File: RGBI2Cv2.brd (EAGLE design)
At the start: 37.8 x 50.8 mm, 10 parts, among them Q1 STP16NF06, Q2 STP16NF06, Q3 STP16NF06, U2 ATTINY45-20PU

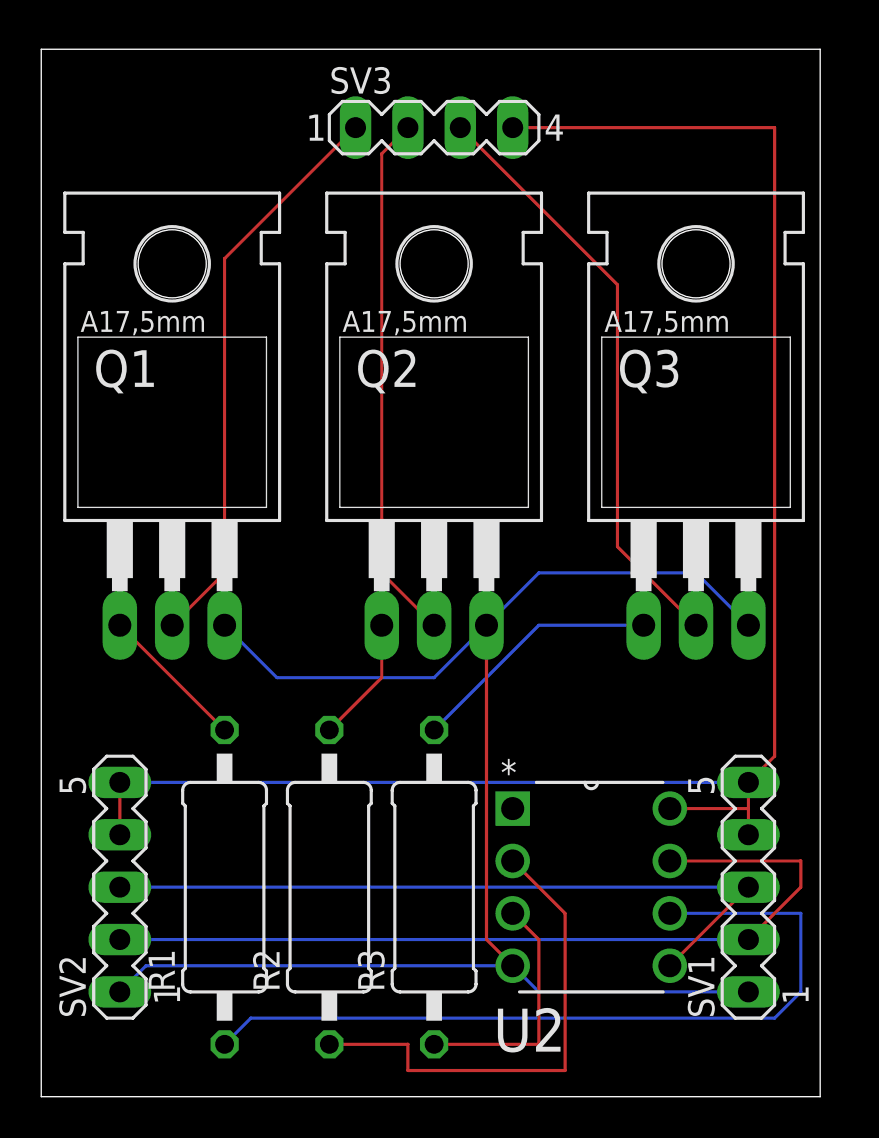
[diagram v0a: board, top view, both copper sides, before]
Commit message: Updated design.
Fixed:
Corrected wiring of in/out headers
Corrected net issue to fix 12v/5v mix
Changed resistor symbol

Added:
Filter caps for ATTiny45
Labled components
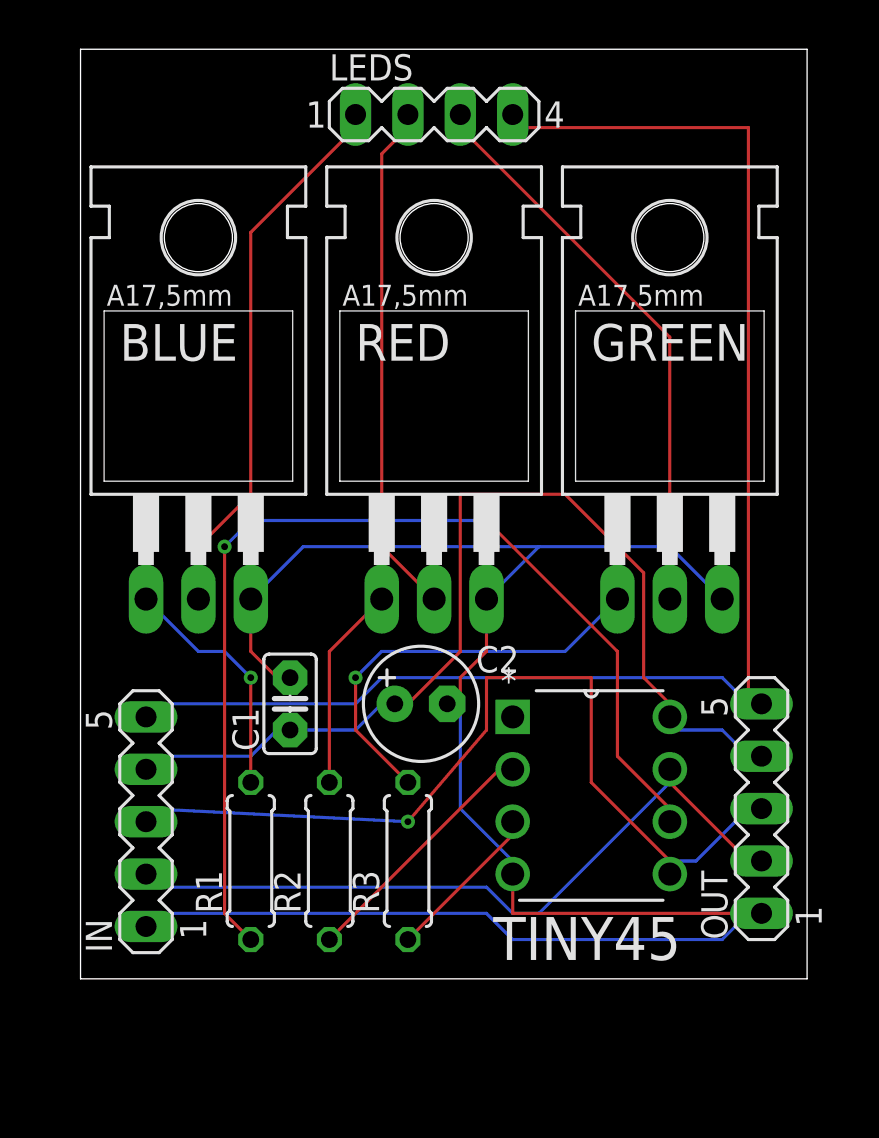
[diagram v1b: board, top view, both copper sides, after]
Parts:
- removed Q1, Q2, Q3: STP16NF06, transistor-power:TO220BH
- removed SV1, SV2: (no value), con-lstb:MA05-1
- removed SV3: (no value), con-lstb:MA04-1
- removed U2: ATTINY45-20PU, Atmel_By_element14_Batch_1:DIP254P762X533-8
- added BLUE, GREEN, RED: STP16NF06, transistor-power:TO220BH
- added C1: 0.1uF, minimidi:C025-025X050
- added C2: 100/6VuF, minimidi:E2,5-6
- added IN, OUT: (no value), con-lstb:MA05-1
- added LEDS: (no value), con-lstb:MA04-1
- added TINY45: ATTINY45-20PU, Atmel_By_element14_Batch_1:DIP254P762X533-8
- R1, R2, R3: device resistor:0411/15 -> rcl:0207/7
- moved R1 1.80 mm to (10.2, 40.6)
- moved R3 1.80 mm to (17.8, 40.6)
- moved R2 1.27 mm to (14.0, 40.6)
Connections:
- removed net VCC: SV1.4, SV1.5, SV2.4, SV2.5, SV3.4, U2.8
- new net 12V: IN.5, LEDS.4, OUT.5
- new net VCC5V: C1.1, C2.+, IN.4, OUT.4, TINY45.8
- net GND: now also BLUE.S, C1.2, C2.-, GREEN.S, IN.1, OUT.1, RED.S, TINY45.4; no longer Q1.S, Q2.S, Q3.S, SV1.1, SV2.1, U2.4
- net N$1: now also BLUE.D, LEDS.1; no longer Q1.D, SV3.1
- net N$10: now also TINY45.3; no longer U2.3
- net N$11: now also GREEN.D, LEDS.3; no longer Q3.D, SV3.3
- net N$2: now also LEDS.2, RED.D; no longer Q2.D, SV3.2
- net N$3: now also IN.2, OUT.2, TINY45.7; no longer SV1.2, SV2.2, U2.7
- net N$4: now also IN.3, OUT.3, TINY45.5; no longer SV1.3, SV2.3, U2.5
- net N$5: now also TINY45.6; no longer U2.6
- net N$6: now also BLUE.G; no longer Q1.G
- net N$7: now also RED.G; no longer Q2.G
- net N$8: now also GREEN.G; no longer Q3.G
- net N$9: now also TINY45.2; no longer U2.2
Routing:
- net VCC: track 84.3 -> 0.00 mm
- net 12V: track 0.00 -> 72.2 mm
- net VCC5V: track 0.00 -> 49.2 mm
- net GND: track 78.2 -> 95.2 mm
- net N$5: track 39.2 -> 51.1 mm, vias 0 -> 2
- net N$9: track 23.9 -> 13.2 mm
- net N$4: track 35.9 -> 44.1 mm, vias 0 -> 1
- net N$8: track 12.3 -> 20.4 mm, vias 0 -> 1
- net N$3: track 41.7 -> 36.5 mm
- net N$6: track 7.18 -> 11.7 mm, vias 0 -> 1
- net N$10: track 12.0 -> 7.82 mm
- net N$7: track 6.13 -> 9.94 mm
- net N$1: track 27.8 -> 26.7 mm
- net N$11: track 28.9 -> 27.7 mm
- net N$2: track 25.7 -> 25.1 mm
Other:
- board size 37.8 x 50.8 mm -> 35.2 x 45.1 mm
